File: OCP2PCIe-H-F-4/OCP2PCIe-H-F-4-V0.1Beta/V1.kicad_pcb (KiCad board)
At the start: 2 copper layers, 112.1 x 78.2 mm, 13 parts, among them J1 PCI Express x4, J2 Conn_02x40_Top_Bottom, J3 Conn_01x02, J4 Conn_01x02, J5 Conn_01x02, J6 Conn_01x02, U1 DM02

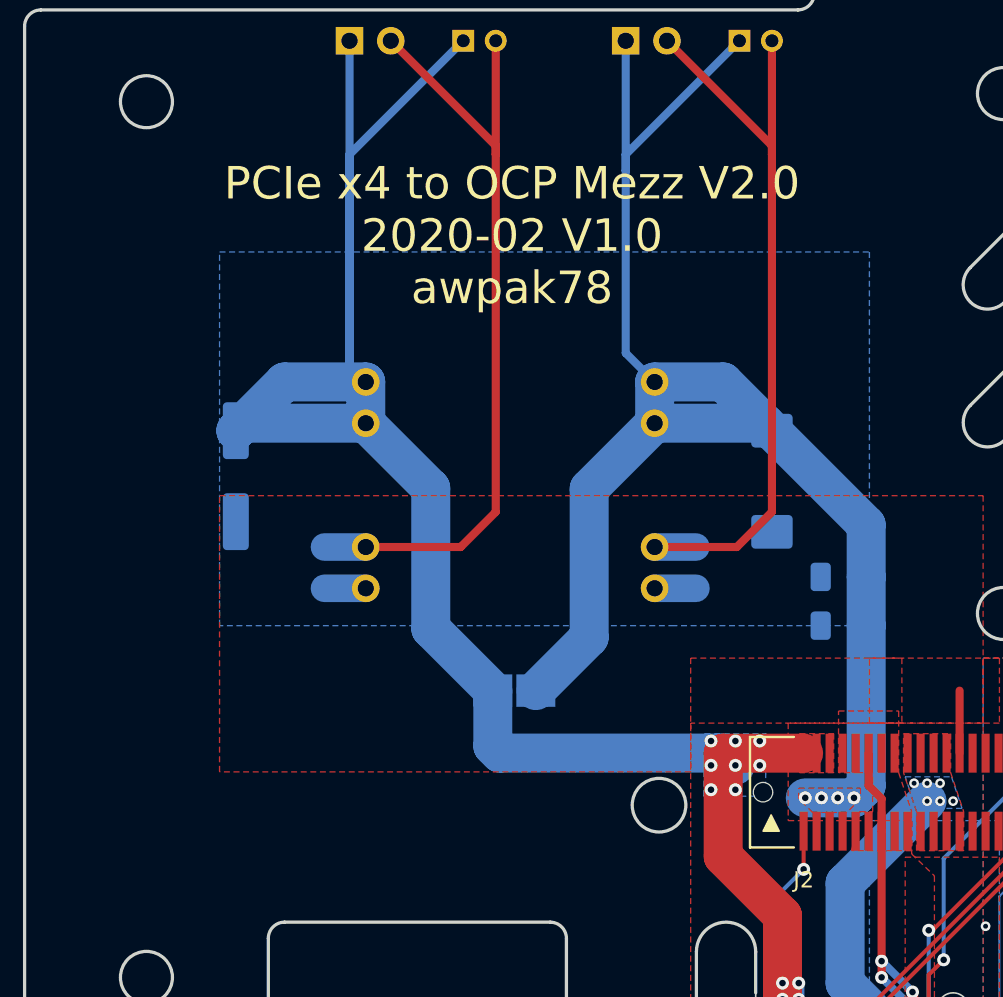
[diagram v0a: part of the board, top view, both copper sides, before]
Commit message: Update OSHW and GNU Logo
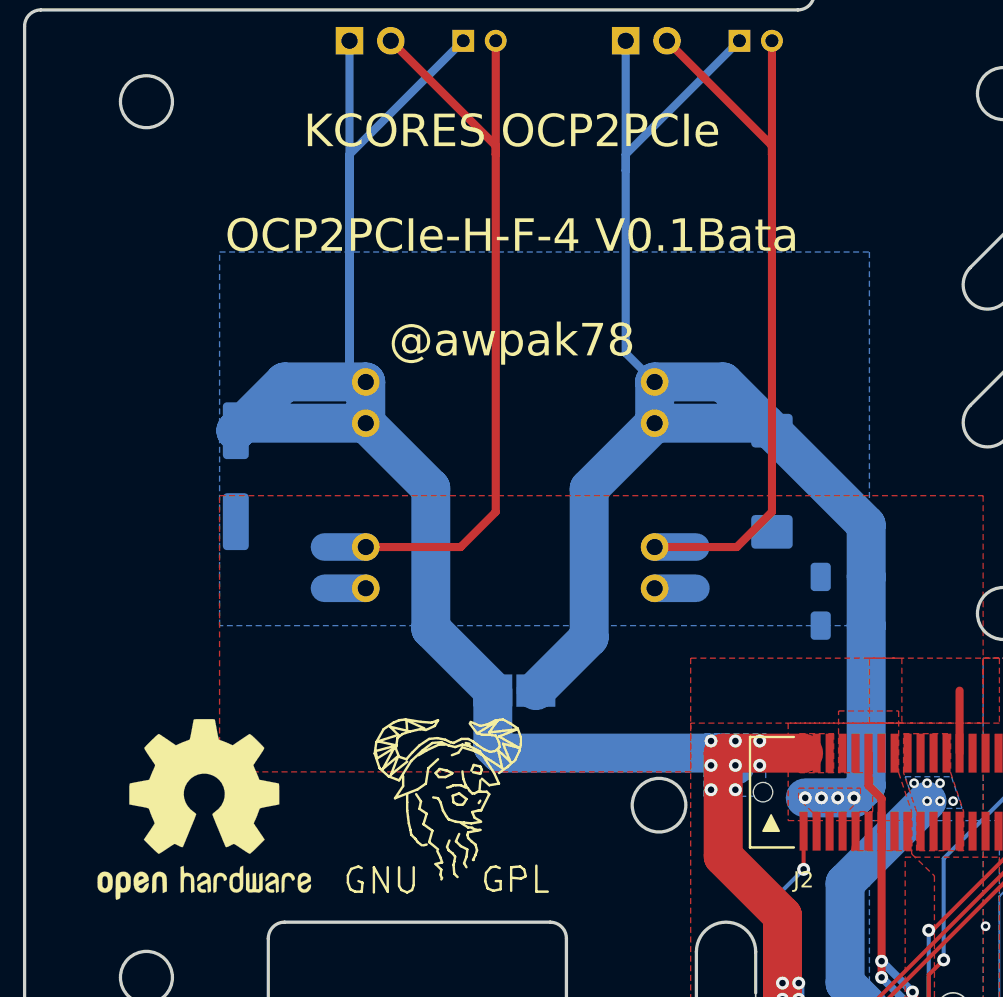
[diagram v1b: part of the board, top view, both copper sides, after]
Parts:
- added REF**: OSHW-Logo2_14.6x12mm_SilkScreen, Symbol:OSHW-Logo2_14.6x12mm_SilkScreen, F.Cu at (99.1, 114.3)
- added REF**: Symbol_GNU-Logo_SilkscreenTop, Symbol:Symbol_GNU-Logo_SilkscreenTop, F.Cu at (114.3, 112.5)
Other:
- board text added: "KCORES OCP2PCIe OCP2PCIe-H-F-4 V0.1Bata @awpak78"
- board text removed: "PCIe x4 to OCP Mezz V2.0 2020-02 V1.0 awpak78"
